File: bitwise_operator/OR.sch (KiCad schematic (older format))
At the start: 4 parts, among them U10 74LS86, U11 74LS86, U12 74LS86, U9 74LS86

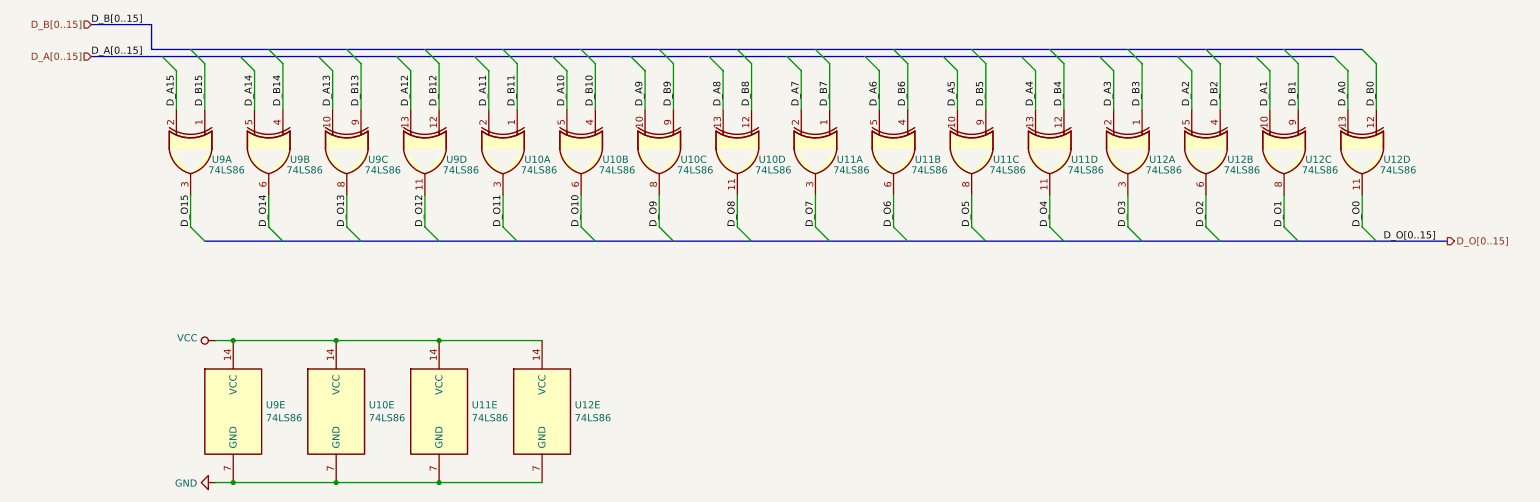
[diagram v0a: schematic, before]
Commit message: add bit operations
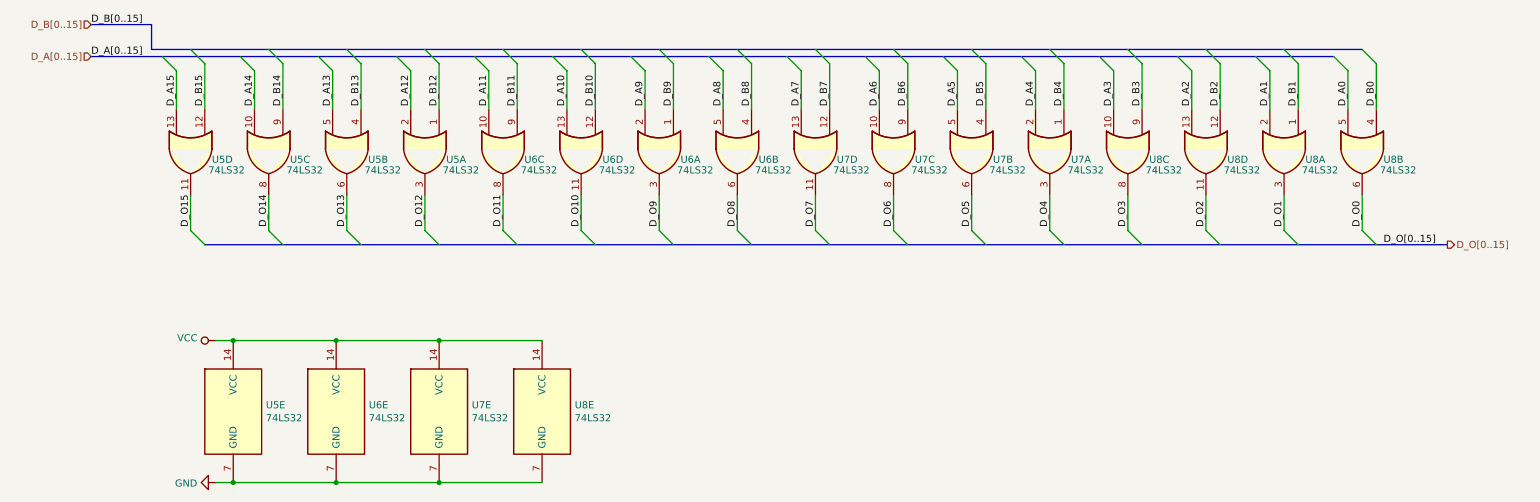
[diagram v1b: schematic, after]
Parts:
- removed U10, U11, U12, U9: 74LS86, Package_DIP:DIP-14_W7.62mm_LongPads, symbol 74xx:74LS86
- added U5, U6, U7, U8: 74LS32, Package_DIP:DIP-14_W7.62mm_LongPads, symbol 74xx:74LS32
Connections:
- net D_A0: now also U8.5
- net D_A1: now also U8.2
- net D_A10: now also U6.13
- net D_A11: now also U6.10
- net D_A12: now also U5.2
- net D_A13: now also U5.5
- net D_A14: now also U5.10
- net D_A15: now also U5.13
- net D_A2: now also U8.13
- net D_A3: now also U8.10
- net D_A4: now also U7.2
- net D_A5: now also U7.5
- net D_A6: now also U7.10
- net D_A7: now also U7.13
- net D_A8: now also U6.5
- net D_A9: now also U6.2
- net D_B0: now also U8.4
- net D_B1: now also U8.1
- net D_B10: now also U6.12
- net D_B11: now also U6.9
- net D_B12: now also U5.1
- net D_B13: now also U5.4
- net D_B14: now also U5.9
- net D_B15: now also U5.12
- net D_B2: now also U8.12
- net D_B3: now also U8.9
- net D_B4: now also U7.1
- net D_B5: now also U7.4
- net D_B6: now also U7.9
- net D_B7: now also U7.12
- net D_B8: now also U6.4
- net D_B9: now also U6.1
- net D_O0: now also U8.6
- net D_O1: now also U8.3
- net D_O10: now also U6.11
- net D_O11: now also U6.8
- net D_O12: now also U5.3
- net D_O13: now also U5.6
- net D_O14: now also U5.8
- net D_O15: now also U5.11
- net D_O2: now also U8.11
- net D_O3: now also U8.8
- net D_O4: now also U7.3
- net D_O5: now also U7.6
- net D_O6: now also U7.8
- net D_O7: now also U7.11
- net D_O8: now also U6.6
- net D_O9: now also U6.3
- net GND: now also U5.7 (GND), U6.7 (GND), U7.7 (GND), U8.7 (GND)
- net VCC: now also U5.14 (VCC), U6.14 (VCC), U7.14 (VCC), U8.14 (VCC)
